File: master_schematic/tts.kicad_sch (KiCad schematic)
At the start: 6 parts, among them U4 MCP9600_Module, U5 MCP9600_Module, U6 MCP9600_Module, U7 MCP9600_Module, U8 MCP9600_Module, U9 MCP9600_Module

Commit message: modified for PCB development
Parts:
- removed U9: MCP9600_Module, symbol hb_symbol_lib:MCP9600_Module
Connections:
- net SCL_1 is gone; now on net SCL: U7.3 (SCL), U8.3 (SCL)
- net SDA_1 is gone; now on net SDA: U7.4 (SDA), U8.4 (SDA)
- no-connect marks 30 -> 25
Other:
- note added: "MCP9600 can be configured to have 5 I2C addresses, which is exactly what we're doing"
- note removed: "Note: using 2 I2C buses, set each device to a different address"

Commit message: updated with part info
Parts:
- U4, U5, U6, U7, U8: footprint (none) -> hb_footprint_lib:mcp9600_connector

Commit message: updated BOM
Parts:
- U4, U5, U6, U7, U8: Cost @ Qty (none) -> 0.63; Manufacturer (none) -> Sullins Connector Solutions; Manufacturer Part # (none) -> PPPC091LFBN-RC; Supplier (none) -> Digikey; Supplier Part # (none) -> PPPC091LFBN-RC; Unit Cost (none) -> 0.63

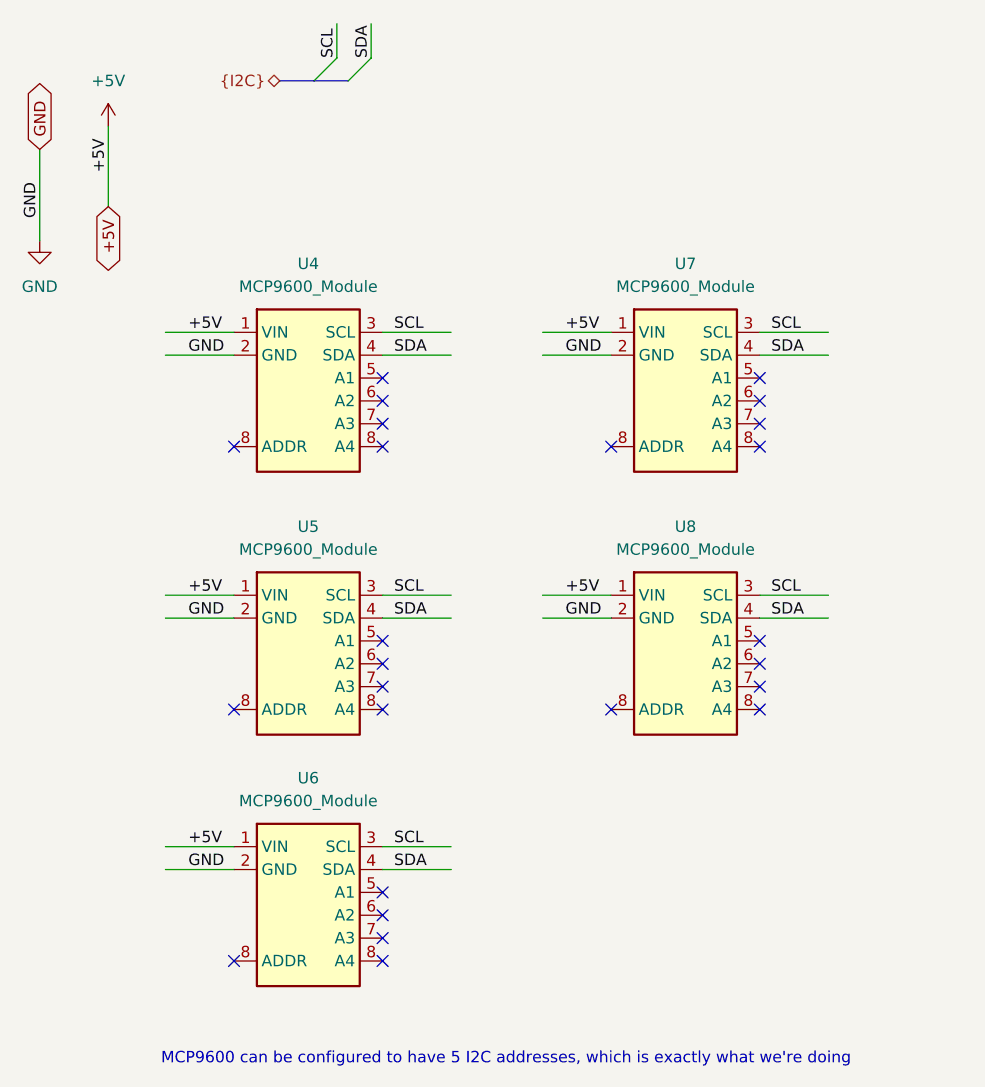
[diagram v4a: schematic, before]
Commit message: added decoupling capacitors, fixed voltage values for TTs and load cells to +3V3
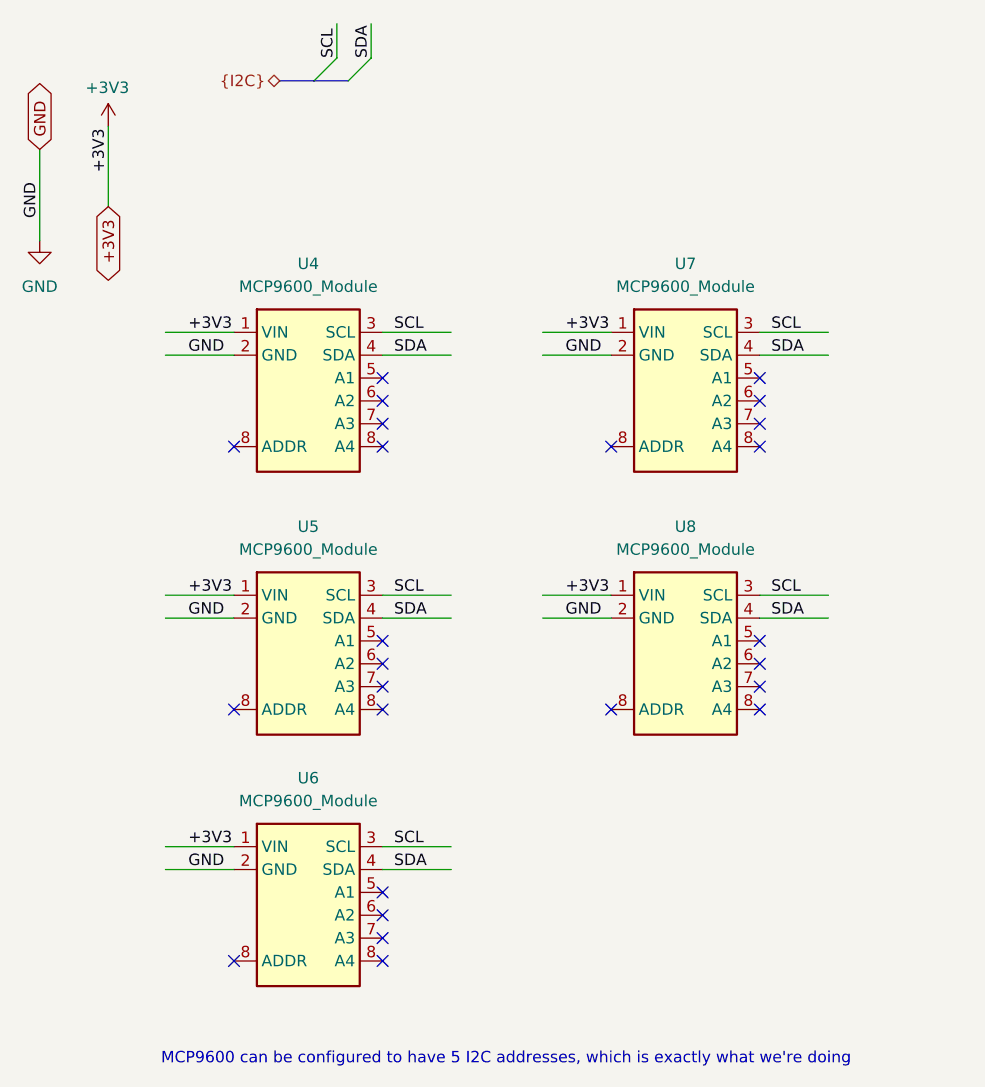
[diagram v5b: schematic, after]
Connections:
- net +5V renamed +3V3
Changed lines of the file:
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@@
 	(wire
 		(pts
-			(xy 36.83 38.1) (xy 36.83 29.21)
+			(xy 36.83 29.21) (xy 36.83 38.1)
 		)
 		(stroke
@@
 		)
 	)
-	(label "+5V"
+	(label "+3V3"
 		(at 45.72 81.28 0)
 		(fields_autoplaced yes)
@@
 		)
 	)
-	(label "+5V"
+	(label "+3V3"
 		(at 87.63 81.28 0)
 		(fields_autoplaced yes)
@@
 		)
 	)
-	(label "+5V"
+	(label "+3V3"
 		(at 36.83 34.29 90)
 		(fields_autoplaced yes)
@@
 		)
 	)
-	(label "+5V"
+	(label "+3V3"
 		(at 45.72 109.22 0)
 		(fields_autoplaced yes)
@@
 		)
 	)
-	(label "+5V"
+	(label "+3V3"
 		(at 45.72 52.07 0)
 		(fields_autoplaced yes)
@@
 		)
 	)
-	(label "+5V"
+	(label "+3V3"
 		(at 87.63 52.07 0)
 		(fields_autoplaced yes)
@@
 		)
 	)
-	(global_label "+5V"
+	(global_label "+3V3"
 		(shape bidirectional)
 		(at 36.83 38.1 270)
@@
 		)
 		(property "Intersheetrefs" "${INTERSHEET_REFS}"
-			(at 36.83 46.067 90)
+			(at 36.83 47.2765 90)
 			(effects
 				(font
@@
 	)
 	(symbol
-		(lib_name "hb_symbol_lib:MCP9600_Module")
 		(lib_id "hb_symbol_lib:MCP9600_Module")
 		(at 101.6 48.26 0)
@@
 	)
 	(symbol
-		(lib_name "hb_symbol_lib:MCP9600_Module")
 		(lib_id "hb_symbol_lib:MCP9600_Module")
 		(at 101.6 77.47 0)
@@
 		(dnp no)
 		(fields_autoplaced yes)
-		(property "Reference" "#PWR046"
+		(property "Reference" "#PWR061"
 			(at 29.21 48.26 0)
 			(effects
@@
 			(project "master_schematic"
 				(path "/c4f7e98c-e88d-49cc-9841-b70710a90a72/ac0b5093-6e20-433c-b604-e10ee3af976c"
-					(reference "#PWR046")
+					(reference "#PWR061")
 					(unit 1)
 				)
@@
 		(on_board yes)
 		(dnp no)
-		(fields_autoplaced yes)
-		(property "Reference" "#PWR047"
+		(property "Reference" "#PWR062"
 			(at 36.83 33.02 0)
 			(effects
@@
 			)
 		)
-		(property "Value" "+5V"
-			(at 36.83 24.13 0)
-			(effects
-				(font
-					(size 1.27 1.27)
-				)
+		(property "Value" "+3V3"
+			(at 34.29 24.892 0)
+			(effects
+				(font
+					(size 1.27 1.27)
+				)
+				(justify left)
 			)
 		)
@@
 			(project "master_schematic"
 				(path "/c4f7e98c-e88d-49cc-9841-b70710a90a72/ac0b5093-6e20-433c-b604-e10ee3af976c"
-					(reference "#PWR047")
+					(reference "#PWR062")
 					(unit 1)
 				)
@@
 	)
 	(symbol
-		(lib_name "hb_symbol_lib:MCP9600_Module")
 		(lib_id "hb_symbol_lib:MCP9600_Module")
 		(at 59.69 77.47 0)
@@
 	)
 	(symbol
-		(lib_name "hb_symbol_lib:MCP9600_Module")
 		(lib_id "hb_symbol_lib:MCP9600_Module")
 		(at 59.69 105.41 0)
@@
 	)
 	(symbol
-		(lib_name "hb_symbol_lib:MCP9600_Module")
 		(lib_id "hb_symbol_lib:MCP9600_Module")
 		(at 59.69 48.26 0)
